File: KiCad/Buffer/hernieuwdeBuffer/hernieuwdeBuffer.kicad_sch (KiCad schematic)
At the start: 38 parts, among them J1 Conn_01x04_Female, J2 12V DC, SW1 ENABLE, SW2 BOOT, T1 signaal oranje, U1 ESP32-WROOM-32E_(16MB)

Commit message: kicad
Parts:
- J3: value (none) -> Rood; footprint (none) -> libraries:TE_282841-5
- J4: value (none) -> Groen; footprint (none) -> libraries:TE_282841-5
- J5: value (none) -> Oranje1; footprint (none) -> libraries:TE_282841-6
- J6: value (none) -> Oranje2; footprint (none) -> libraries:TE_282841-6
- R1: footprint libraries:RESC6332X65N -> (none)
- T10: value (none) -> o3r
- T11: value (none) -> o4r
- T12: value (none) -> o5r
- T13: value (none) -> 06r
- T14: value (none) -> r1
- T15: value (none) -> r2
- T16: value (none) -> r3
- T17: value (none) -> r4
- T18: value (none) -> r5
- T19: value (none) -> g1
- T2: value (none) -> o1g
- T20: value (none) -> g2
- T21: value (none) -> g3
- T22: value (none) -> g4
- T23: value (none) -> g5
- T3: value (none) -> o2g
- T4: value (none) -> o3g
- T5: value (none) -> o4g
- T6: value (none) -> o5g
- T7: value (none) -> 06g
- T8: value (none) -> o1r
- T9: value (none) -> o2r

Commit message: updates standaard schema
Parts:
- added R2: 10k, libraries:RESC6332X65N, symbol Device:R
- PS1: value ITX0512SA -> (none); footprint libraries:Buck Converter -> (none)
- R1: footprint (none) -> libraries:RESC6332X65N
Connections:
- net +3V3: now also R1.1, R2.1
- net at C1.2, SW1.1, SW1.2: now also R1.2, U1.3 (EN); no longer R1.1
- net at SW2.1, SW2.2, U1.25 (IO0): now also R2.2

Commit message: kicad aanpassingen buffer
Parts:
- R1, R2: footprint libraries:RESC6332X65N -> (none)
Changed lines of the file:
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@@
       (effects (font (size 1.27 1.27)) (justify left))
     )
-    (property "Footprint" "libraries:RESC6332X65N" (id 2) (at 42.672 54.61 90)
+    (property "Footprint" "" (id 2) (at 42.672 54.61 90)
       (effects (font (size 1.27 1.27)) hide)
     )
@@
       (effects (font (size 1.27 1.27)) (justify left))
     )
-    (property "Footprint" "libraries:RESC6332X65N" (id 2) (at 88.392 46.99 90)
+    (property "Footprint" "" (id 2) (at 88.392 46.99 90)
       (effects (font (size 1.27 1.27)) hide)
     )
@@
     )
     (path "/9d072175-6cd4-46e7-8845-1132e5fc1b17"
-      (reference "R1") (unit 1) (value "10k") (footprint "libraries:RESC6332X65N")
+      (reference "R1") (unit 1) (value "10k") (footprint "Resistor_SMD:R_0805_2012Metric")
     )
     (path "/b5e37d81-054e-45c5-b61e-117b78654e64"
-      (reference "R2") (unit 1) (value "10k") (footprint "libraries:RESC6332X65N")
+      (reference "R2") (unit 1) (value "10k") (footprint "Resistor_SMD:R_0805_2012Metric")
     )
     (path "/3d23cf47-7cc8-4c1d-b5fd-e2d35ca14dd8"

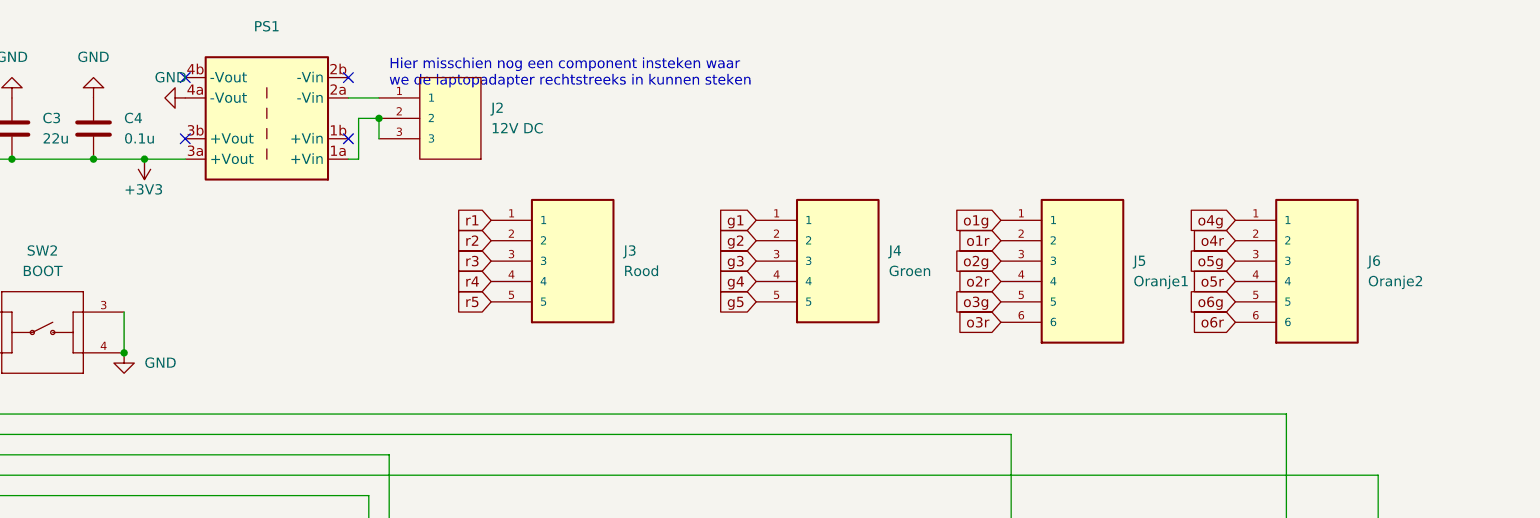
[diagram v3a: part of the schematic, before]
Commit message: update buffer
enkel schema van de buffer is volledig in orde met LDO!!!
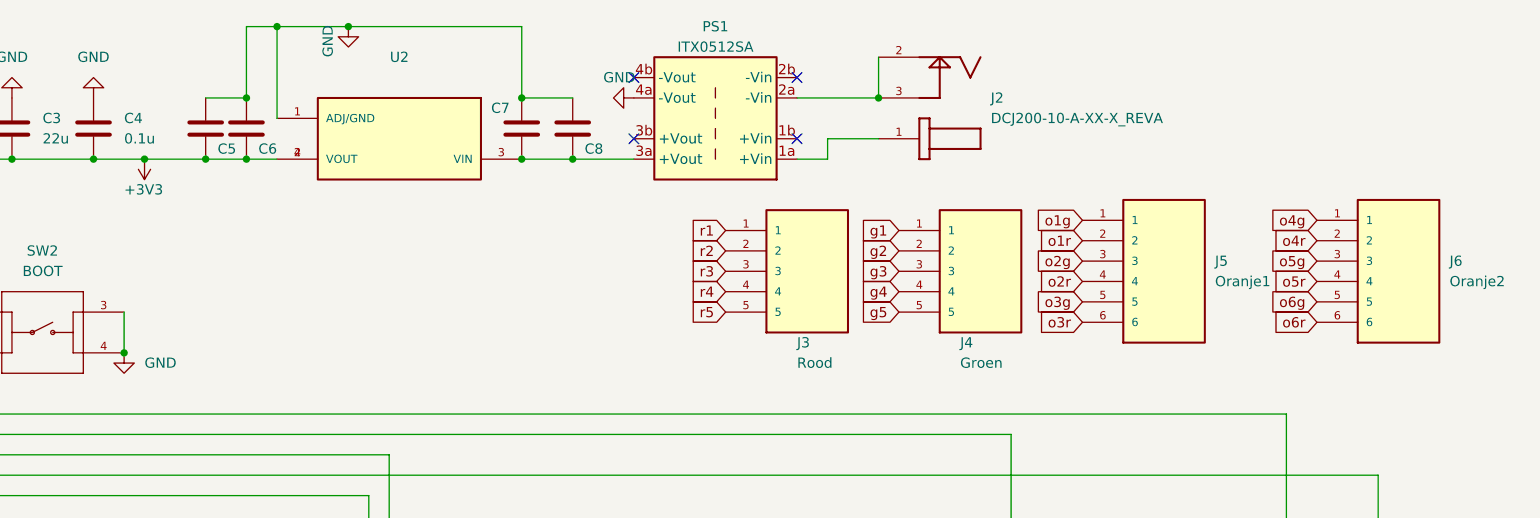
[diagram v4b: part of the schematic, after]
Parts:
- removed J2: 12V DC, libraries:TE_282841-3, symbol 282841-3:282841-3
- added C5, C6, C7, C8: (no value), symbol Device:C
- added J2: DCJ200-10-A-XX-X_REVA, libraries:GCT_DCJ200-10-A-XX-X_REVA, symbol DCJ200-10-A-XX-X_REVA:DCJ200-10-A-XX-X_REVA
- added U2: (no value), symbol AMS1117:AMS1117
- C2: footprint Capacitor_SMD:C_0805_2012Metric -> libraries:CAP_EEE0JA101WR
- PS1: value (none) -> ITX0512SA; footprint (none) -> libraries:Buck Converter
- R1, R2: footprint (none) -> Resistor_SMD:R_0805_2012Metric
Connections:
- net +3V3: now also C5.1, C6.1, U2.2 (VOUT), U2.4 (VOUT); no longer PS1.3a (+Vout)
- net GND: now also C5.2, C6.2, C7.1, C8.2, U2.1 (ADJ/GND)
- net at PS1.2a (-Vin): now also J2.2, J2.3
- net at PS1.1a (+Vin): now also J2.1
- new net: C7.2, C8.1, PS1.3a (+Vout), U2.3 (VIN)
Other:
- note removed: "Hier misschien nog een component insteken waar we de laptopadapter rechtstreeks in kunnen steken"
- moved on the sheet: J3, J4, J5, J6, PS1

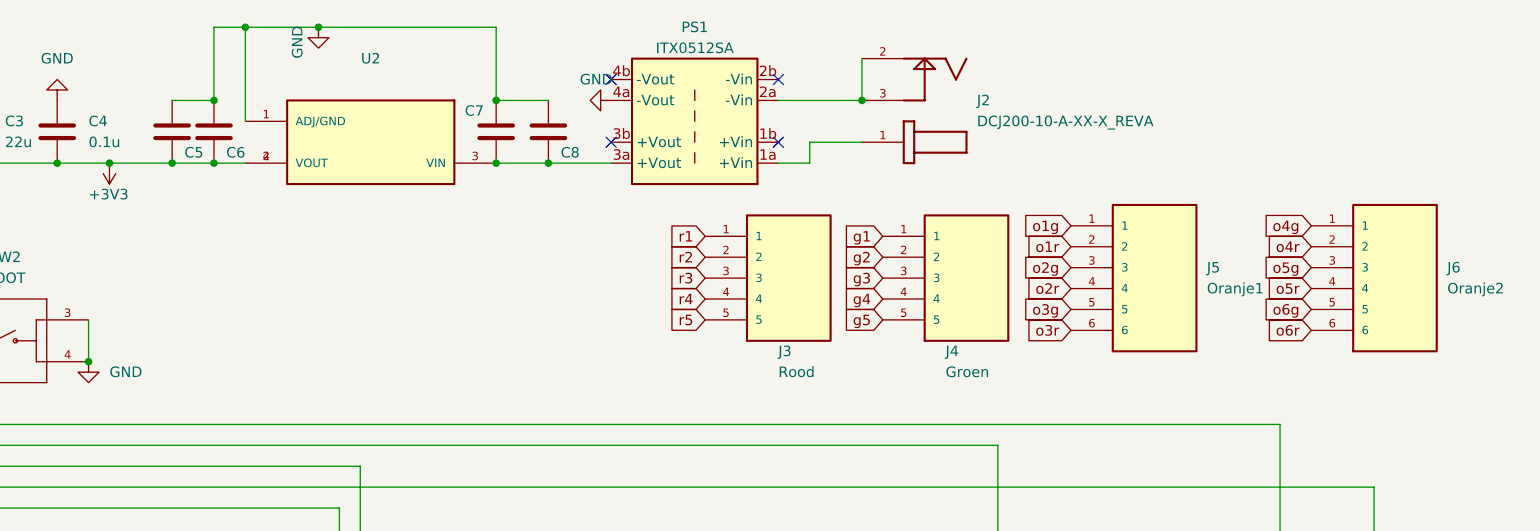
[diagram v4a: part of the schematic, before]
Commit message: updaten van 7 segment ground plane(s)
versie voor 7 segment met 1 ground plane aan achterkant en andere versie met ground plane aan voor- en achterkant
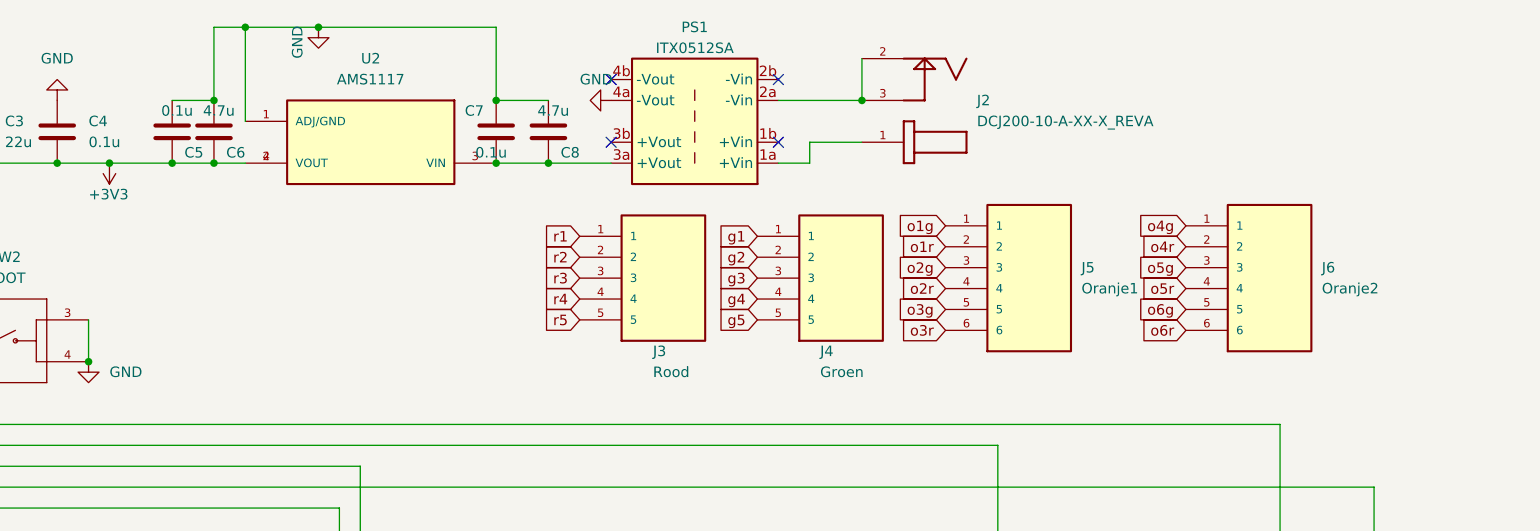
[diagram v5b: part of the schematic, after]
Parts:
- C5, C7: value (none) -> 0.1u; footprint (none) -> Capacitor_SMD:C_0805_2012Metric
- C6, C8: value (none) -> 4.7u; footprint (none) -> Capacitor_SMD:C_0805_2012Metric
- U2: value (none) -> AMS1117; footprint (none) -> libraries:SOT229P700X180-4N
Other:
- moved on the sheet: J3, J4, J5, J6

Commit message: aanpassingen aan kicad ontwerpen van 7segment en buffer
toevoeging van groundplanes
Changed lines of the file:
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@@
   (junction (at 166.37 24.13) (diameter 0) (color 0 0 0 0)
   )
+  (junction (at 87.63 36.83) (diameter 0) (color 0 0 0 0)
+  )
   (junction (at 102.87 31.75) (diameter 0) (color 0 0 0 0)
   )
   (junction (at 127 121.92) (diameter 0) (color 0 0 0 0)
-  )
-  (junction (at 119.38 31.75) (diameter 0) (color 0 0 0 0)
   )
   (junction (at 90.17 50.8) (diameter 0) (color 0 0 0 0)
@@
     (stroke (width 0) (type default) (color 0 0 0 0))
   )
-  (wire (pts (xy 87.63 31.75) (xy 87.63 53.34))
+  (wire (pts (xy 87.63 31.75) (xy 87.63 36.83))
     (stroke (width 0) (type default) (color 0 0 0 0))
   )
@@
     (stroke (width 0) (type default) (color 0 0 0 0))
   )
-  (wire (pts (xy 119.38 31.75) (xy 113.03 31.75))
+  (wire (pts (xy 113.03 31.75) (xy 127 31.75))
     (stroke (width 0) (type default) (color 0 0 0 0))
   )
@@
     (stroke (width 0) (type default) (color 0 0 0 0))
   )
+  (wire (pts (xy 87.63 36.83) (xy 87.63 53.34))
+    (stroke (width 0) (type default) (color 0 0 0 0))
+  )
   (wire (pts (xy 21.59 63.5) (xy 21.59 58.42))
     (stroke (width 0) (type default) (color 0 0 0 0))
@@
   )
   (wire (pts (xy 101.6 154.94) (xy 101.6 167.64))
-    (stroke (width 0) (type default) (color 0 0 0 0))
-  )
-  (wire (pts (xy 119.38 31.75) (xy 127 31.75))
     (stroke (width 0) (type default) (color 0 0 0 0))
   )
@@
     (pin "2")
   )
-  (symbol (lib_id "power:+3V3") (at 119.38 31.75 180) (unit 1)
-    (in_bom yes) (on_board yes)
-    (property "Reference" "#PWR0122" (id 0) (at 119.38 27.94 0)
-      (effects (font (size 1.27 1.27)) hide)
-    )
-    (property "Value" "+3V3" (id 1) (at 116.84 35.56 0)
-      (effects (font (size 1.27 1.27)) (justify right))
-    )
-    (property "Footprint" "" (id 2) (at 119.38 31.75 0)
-      (effects (font (size 1.27 1.27)) hide)
-    )
-    (property "Datasheet" "" (id 3) (at 119.38 31.75 0)
-      (effects (font (size 1.27 1.27)) hide)
-    )
+  (symbol (lib_id "power:+3V3") (at 87.63 36.83 90) (unit 1)
+    (in_bom yes) (on_board yes)
+    (property "Reference" "#PWR0122" (id 0) (at 91.44 36.83 0)
+      (effects (font (size 1.27 1.27)) hide)
+    )
+    (property "Value" "+3V3" (id 1) (at 83.82 34.29 0)
+      (effects (font (size 1.27 1.27)) (justify right))
+    )
+    (property "Footprint" "" (id 2) (at 87.63 36.83 0)
+      (effects (font (size 1.27 1.27)) hide)
+    )
+    (property "Datasheet" "" (id 3) (at 87.63 36.83 0)
+      (effects (font (size 1.27 1.27)) hide)
+    )

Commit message: aanpassingen 11/04 kicad
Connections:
- net GND: now also J2.2, J2.3, PS1.2a (-Vin)
- no-connect marks 10 -> 11
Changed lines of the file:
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@@
   (junction (at 106.68 106.68) (diameter 0) (color 0 0 0 0)
+  )
+  (junction (at 204.47 24.13) (diameter 0) (color 0 0 0 0)
   )
   (no_connect (at 87.63 60.96))
@@
   (no_connect (at 46.99 66.04))
   (no_connect (at 180.34 29.21))
+  (no_connect (at 207.01 24.13))
   (no_connect (at 46.99 68.58))
   (no_connect (at 200.66 29.21))
@@
     (stroke (width 0) (type default) (color 0 0 0 0))
   )
+  (wire (pts (xy 204.47 24.13) (xy 210.82 24.13))
+    (stroke (width 0) (type default) (color 0 0 0 0))
+  )
   (wire (pts (xy 106.68 175.26) (xy 106.68 172.72))
     (stroke (width 0) (type default) (color 0 0 0 0))
@@
     (stroke (width 0) (type default) (color 0 0 0 0))
   )
-  (wire (pts (xy 200.66 24.13) (xy 210.82 24.13))
+  (wire (pts (xy 200.66 24.13) (xy 204.47 24.13))
     (stroke (width 0) (type default) (color 0 0 0 0))
   )
@@
     (pin "1")
   )
+  (symbol (lib_id "power:GND") (at 204.47 24.13 180) (unit 1)
+    (in_bom yes) (on_board yes)
+    (property "Reference" "#PWR?" (id 0) (at 204.47 17.78 0)
+      (effects (font (size 1.27 1.27)) hide)
+    )
+    (property "Value" "GND" (id 1) (at 207.01 20.32 90)
+      (effects (font (size 1.27 1.27)) (justify left))
+    )
+    (property "Footprint" "" (id 2) (at 204.47 24.13 0)
+      (effects (font (size 1.27 1.27)) hide)
+    )
+    (property "Datasheet" "" (id 3) (at 204.47 24.13 0)
+      (effects (font (size 1.27 1.27)) hide)
+    )
+    (pin "1")
+  )
   (symbol (lib_id "Device:C") (at 31.75 71.12 90) (unit 1)
     (in_bom yes) (on_board yes) (fields_autoplaced)
@@
       (reference "#PWR0130") (unit 1) (value "GND") (footprint "")
     )
+    (path "/92632a21-a6ce-4e85-ab43-a528b997c0c2"
+      (reference "#PWR?") (unit 1) (value "GND") (footprint "")
+    )
     (path "/931e0314-2895-41b4-ade0-aa160700a4f7"
